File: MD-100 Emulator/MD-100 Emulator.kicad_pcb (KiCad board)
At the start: 2 copper layers, 106.7 x 72.4 mm, 48 parts, among them J1 CPB_Connector, J2 I2CConn, J3 ICSP, Q1 NPN, U1 24LC1025, U2 24LC1025, U3 24LC1025, U4 24LC1025, U5 74HC00, U6 74HC02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

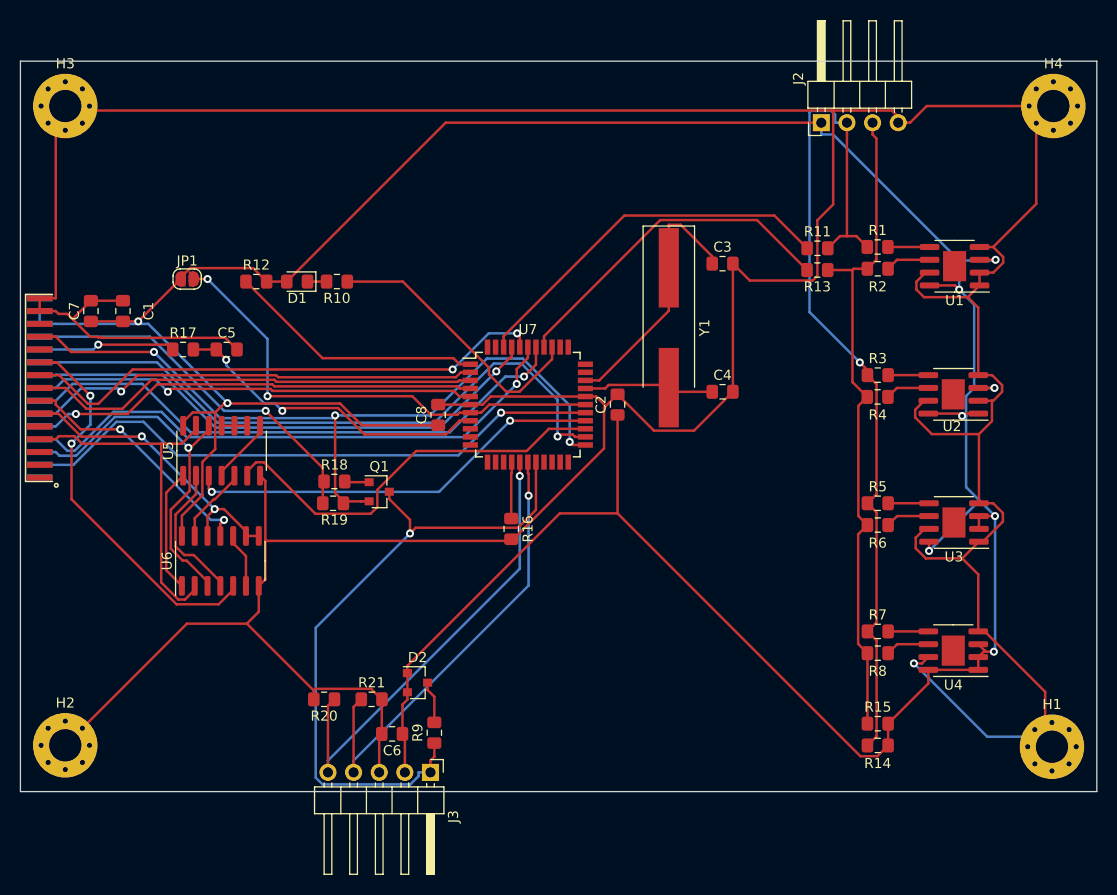
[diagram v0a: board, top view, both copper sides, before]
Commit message: Routage du PCB MD-100 terminé
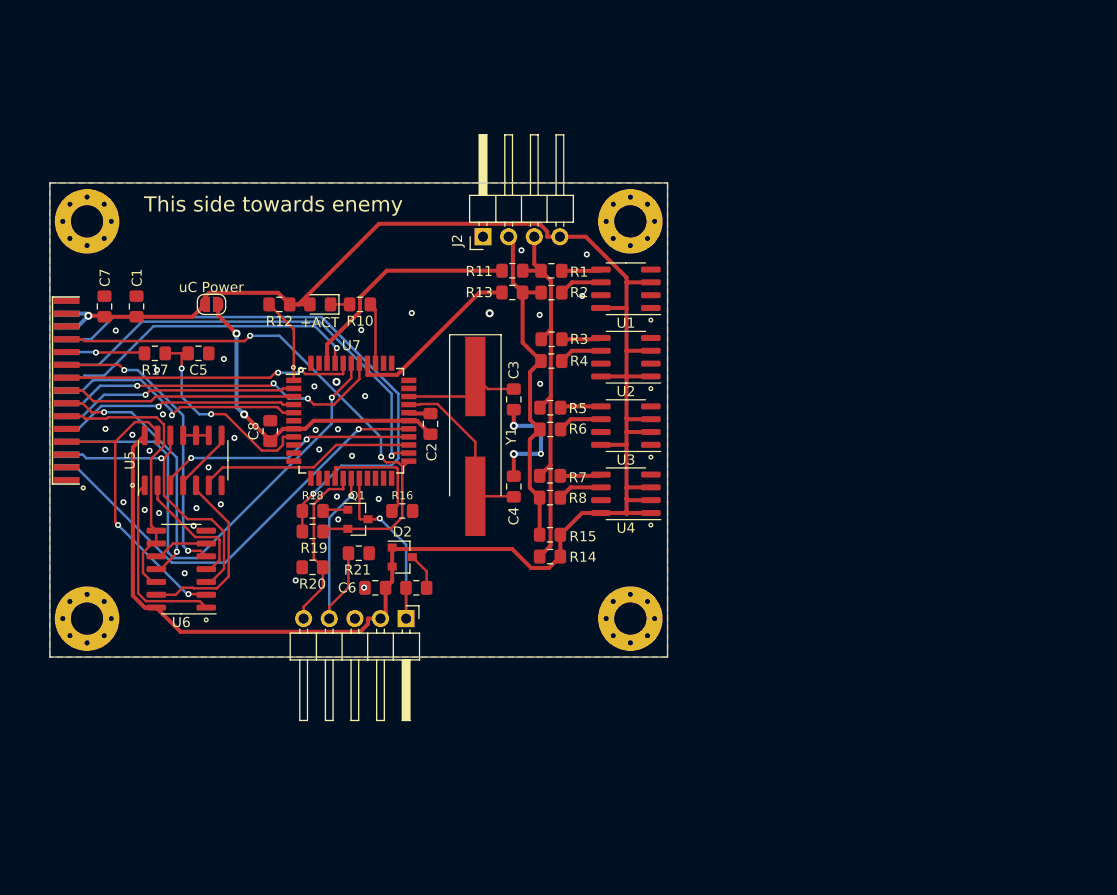
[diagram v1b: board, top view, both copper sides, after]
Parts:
- U1, U2, U3, U4: footprint Package_SO:SOIC-8-1EP_3.9x4.9mm_P1.27mm_EP2.29x3mm -> Package_SO:SOIC-8_3.9x4.9mm_P1.27mm
- moved H1 43.7 mm to (144.9, 134.6)
- moved H4 43.5 mm to (144.9, 95.2)
- moved R14 37.5 mm to (136.9, 128.5)
- moved R15 37.5 mm to (136.9, 126.3)
- moved U4 36.0 mm to (144.5, 122.2)
- moved R8 36.0 mm to (136.9, 122.6)
- moved R7 36.0 mm to (136.9, 120.5)
- moved J2 35.4 mm to (130.3, 96.8)
- moved U3 33.9 mm to (144.5, 115.5)
- moved R5 33.8 mm to (137.0, 113.7)
- moved R6 33.8 mm to (137.0, 115.9)
- moved U2 32.7 mm to (144.5, 108.7)
- moved U1 32.7 mm to (144.5, 101.9)
- moved R3 32.5 mm to (137.1, 106.9)
- moved R4 32.5 mm to (137.1, 109.1)
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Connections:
- net Net-(R1-Pad2) renamed /EE1D
- net Net-(R11-Pad2) renamed /uCD
- net Net-(R13-Pad2) renamed /uCC
- net Net-(R2-Pad2) renamed /EE1C
- net Net-(R3-Pad2) renamed /EE2D
- net Net-(R4-Pad2) renamed /EE2C
- net Net-(R5-Pad2) renamed /EE3D
- net Net-(R6-Pad2) renamed /EE3C
- net Net-(R7-Pad2) renamed /EE4D
- net Net-(R8-Pad2) renamed /EE4C
- C2 pad 1: VCC -> VDD
- C8 pad 1: VCC -> VDD
- J2 pad 1: VCC -> GND
- J2 pad 2: SDA -> SCL
- J2 pad 3: SCL -> SDA
- J2 pad 4: GND -> VCC
- JP1 pad 2: /VDD -> VDD
- U7 pad 28: /VDD -> VDD
- U7 pad 7: /VDD -> VDD
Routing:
- net GND: track 498.0 -> 13.8 mm, vias 1 -> 40
- net VCC: track 338.5 -> 196.1 mm, vias 9 -> 1
- net SDA: track 88.2 -> 39.8 mm, vias 1 -> 0
- net /VDD: track 48.1 -> 0.00 mm, vias 2 -> 0
- net ~MCLR: track 66.7 -> 20.1 mm
- net VDD: track 0.00 -> 33.2 mm, vias 0 -> 2
- net SCL: track 66.1 -> 34.4 mm
- net PGC: track 46.1 -> 17.1 mm, vias 1 -> 0
- net /D2: track 52.9 -> 29.0 mm
- net PGD: track 45.5 -> 22.1 mm
- net /D0: track 56.4 -> 33.3 mm, vias 1 -> 3
- net P3: track 77.1 -> 54.4 mm, vias 3 -> 2
- net /D5: track 44.9 -> 23.2 mm
- net Net-(R10-Pad1): track 27.7 -> 6.04 mm
- net /D3: track 52.9 -> 31.4 mm
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- added copper zone on B.Cu, net GND
- added copper zone on F.Cu, net GND
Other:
- board size 106.7 x 72.4 mm -> 61.2 x 47 mm
- net class Default: via_dia 0.8 -> 0.6; via_drill 0.4 -> 0.3
- net class pwr added: clearance 0.2, trace_width 0.4, via_dia 0.8, via_drill 0.4
- board text added: "+ACT"
- board text added: "This side towards enemy"
- board text added: "uC Power"
